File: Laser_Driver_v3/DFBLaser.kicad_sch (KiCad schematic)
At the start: 30 parts, among them Q15 IRLML6344TRPBF, Q16 IRLML6344TRPBF, U23 OPA192, U24 OPA192

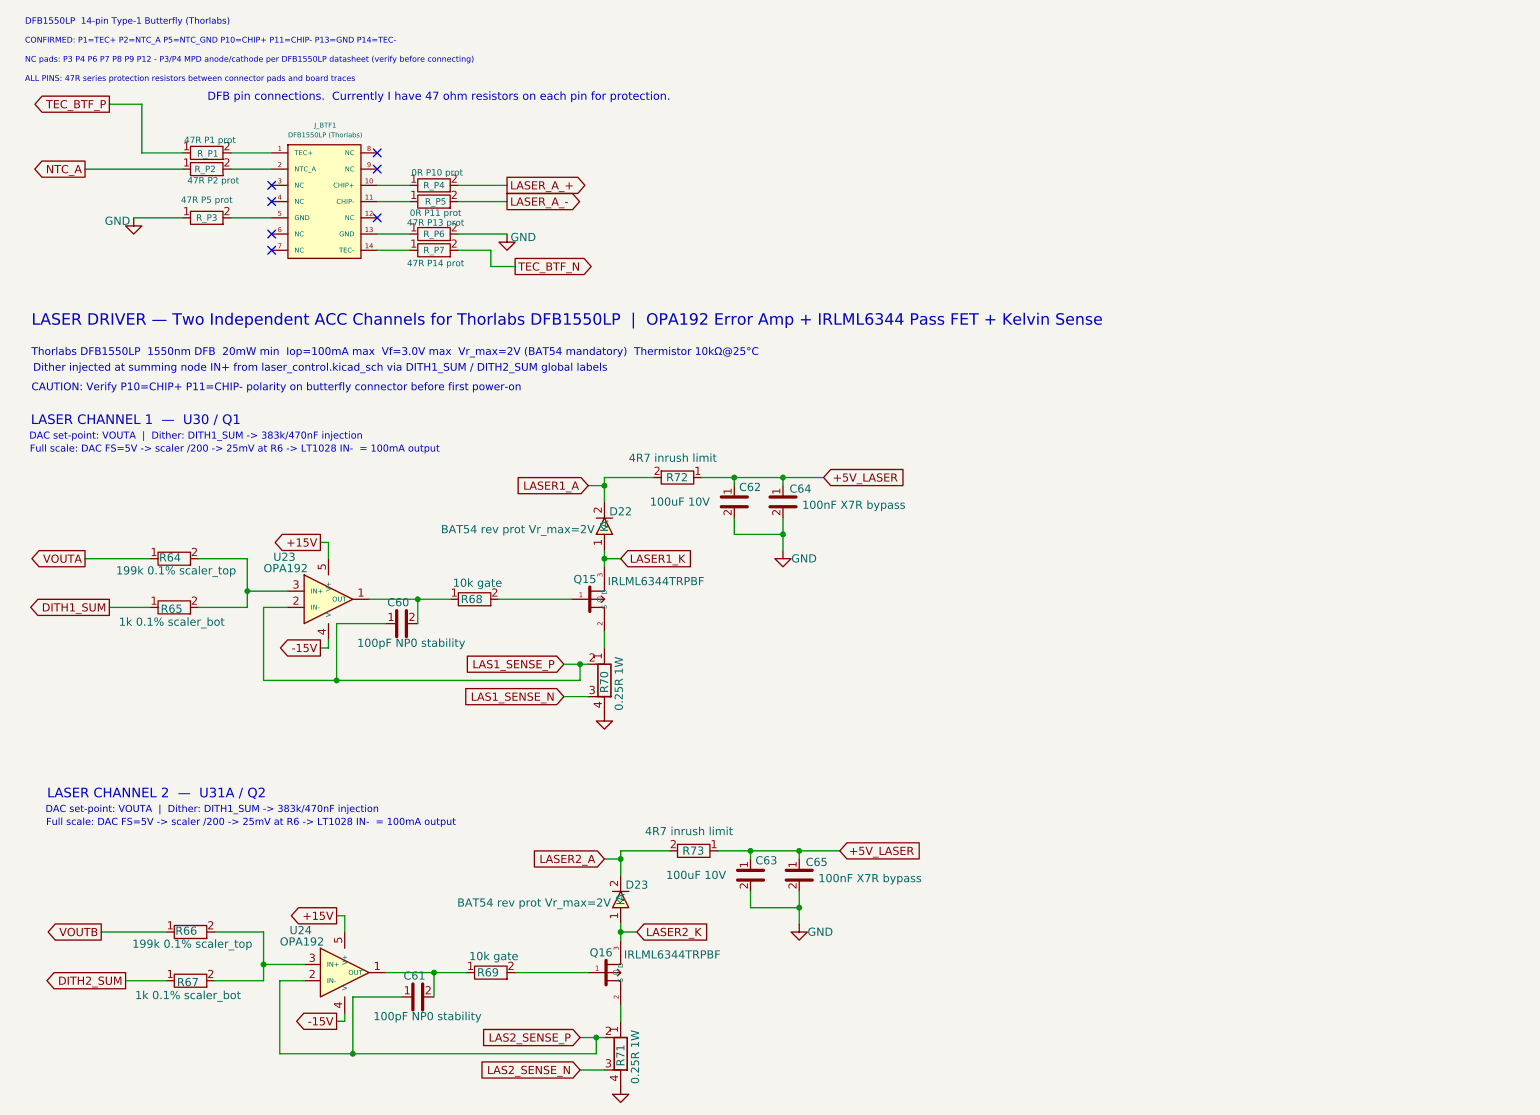
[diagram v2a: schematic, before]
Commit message: Update names, footprints, values, and created BOM
Updated files names, foot prints, component values, parts.
Assigned values from Digikey catalog.
Created CSV BOMs for each schematic.
Including a Power analysis now for all components.
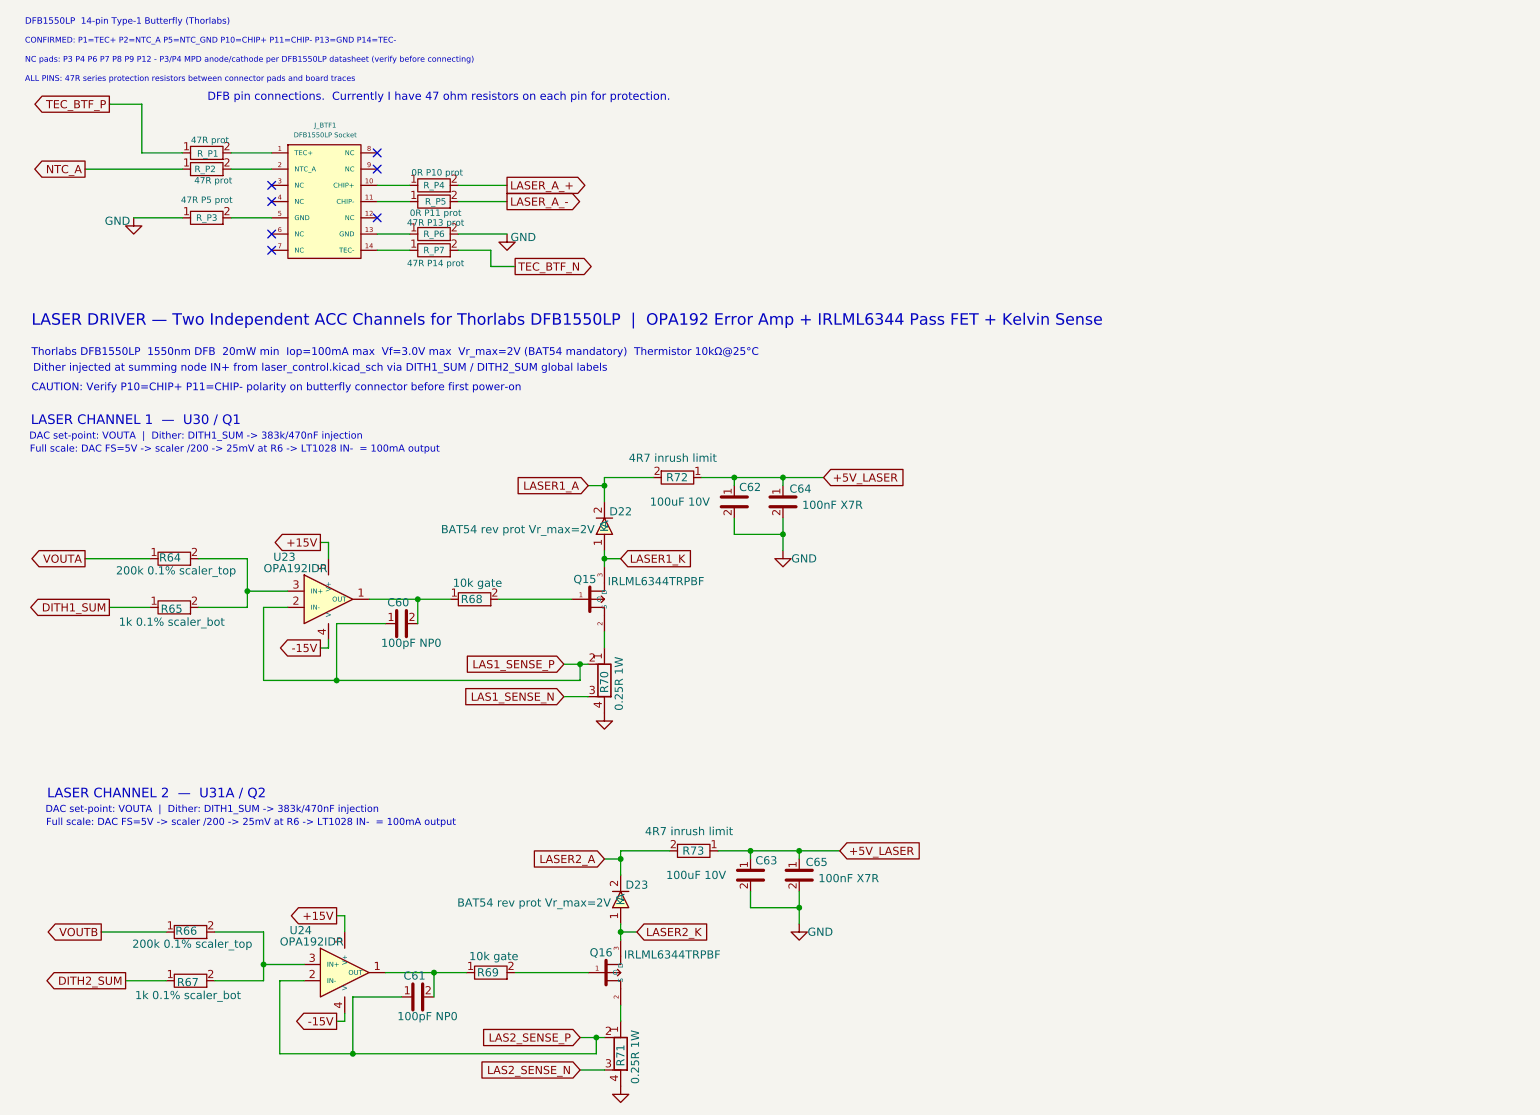
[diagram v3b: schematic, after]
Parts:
- C60, C61: value 100pF NP0 stability -> 100pF NP0; footprint Capacitor_SMD:C_0402_1005Metric -> Capacitor_SMD:C_0805_2012Metric_Pad1.18x1.45mm_HandSolder
- C64, C65: value 100nF X7R bypass -> 100nF X7R; footprint Capacitor_SMD:C_0402_1005Metric -> Capacitor_SMD:C_0805_2012Metric_Pad1.18x1.45mm_HandSolder
- J_BTF1: value DFB1550LP (Thorlabs) -> DFB1550LP Socket; footprint Connector_PinHeader_2.54mm:PinHeader_2x07_P2.54mm_Vertical -> Connector_PinSocket_2.54mm:PinSocket_2x07_P2.54mm_Vertical
- R64, R66: value 199k 0.1% scaler_top -> 200k 0.1% scaler_top
- R68, R69, R_P3, R_P4, R_P5, R_P6, R_P7: footprint Resistor_SMD:R_0402_1005Metric -> Resistor_SMD:R_0805_2012Metric_Pad1.20x1.40mm_HandSolder
- R_P1: value 47R P1 prot -> 47R prot; footprint Resistor_SMD:R_0402_1005Metric -> Resistor_SMD:R_0805_2012Metric_Pad1.20x1.40mm_HandSolder
- R_P2: value 47R P2 prot -> 47R prot; footprint Resistor_SMD:R_0402_1005Metric -> Resistor_SMD:R_0805_2012Metric_Pad1.20x1.40mm_HandSolder
- U23, U24: value OPA192 -> OPA192IDR; footprint Package_SO:SOIC-5-6_4.4x3.6mm_P1.27mm -> Package_SO:SOIC-8_3.9x4.9mm_P1.27mm
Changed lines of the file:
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@@
 			)
 		)
-		(property "Value" "47R P1 prot"
+		(property "Value" "47R prot"
 			(at 44.95 33.56 90)
 			(show_name no)
@@
 			)
 		)
-		(property "Footprint" "Resistor_SMD:R_0402_1005Metric"
+		(property "Footprint" "Resistor_SMD:R_0805_2012Metric_Pad1.20x1.40mm_HandSolder"
 			(at -285.55 73.56 0)
 			(hide yes)
@@
 			)
 		)
-		(property "Footprint" "Resistor_SMD:R_0402_1005Metric"
+		(property "Footprint" "Resistor_SMD:R_0805_2012Metric_Pad1.20x1.40mm_HandSolder"
 			(at 88.9 163.83 0)
 			(hide yes)
@@
 			)
 		)
-		(property "Value" "100pF NP0 stability"
+		(property "Value" "100pF NP0"
 			(at 76.454 112.268 90)
 			(show_name no)
@@
 			)
 		)
-		(property "Footprint" "Capacitor_SMD:C_0402_1005Metric"
+		(property "Footprint" "Capacitor_SMD:C_0805_2012Metric_Pad1.18x1.45mm_HandSolder"
 			(at 74.93 109.22 0)
 			(hide yes)
@@
 			)
 		)
-		(property "Value" "OPA192"
+		(property "Value" "OPA192IDR"
 			(at 53.34 100.584 0)
 			(show_name no)
@@
 			)
 		)
-		(property "Footprint" "Package_SO:SOIC-5-6_4.4x3.6mm_P1.27mm"
+		(property "Footprint" "Package_SO:SOIC-8_3.9x4.9mm_P1.27mm"
 			(at 68.326 87.884 0)
 			(hide yes)
@@
 			)
 		)
-		(property "Footprint" "Resistor_SMD:R_0402_1005Metric"
+		(property "Footprint" "Resistor_SMD:R_0805_2012Metric_Pad1.20x1.40mm_HandSolder"
 			(at -261.99 130.26 0)
 			(hide yes)
@@
 			)
 		)
-		(property "Value" "100nF X7R bypass"
+		(property "Value" "100nF X7R"
 			(at 140.16 149.09 0)
 			(show_name no)
@@
 			)
 		)
-		(property "Footprint" "Capacitor_SMD:C_0402_1005Metric"
+		(property "Footprint" "Capacitor_SMD:C_0805_2012Metric_Pad1.18x1.45mm_HandSolder"
 			(at 137.16 148.59 0)
 			(hide yes)
@@
 			)
 		)
-		(property "Value" "100pF NP0 stability"
+		(property "Value" "100pF NP0"
 			(at 78.994 170.688 90)
 			(show_name no)
@@
 			)
 		)
-		(property "Footprint" "Capacitor_SMD:C_0402_1005Metric"
+		(property "Footprint" "Capacitor_SMD:C_0805_2012Metric_Pad1.18x1.45mm_HandSolder"
 			(at 77.47 167.64 0)
 			(hide yes)
@@
 			)
 		)
-		(property "Value" "47R P2 prot"
+		(property "Value" "47R prot"
 			(at 45.466 39.878 90)
 			(show_name no)
@@
 			)
 		)
-		(property "Footprint" "Resistor_SMD:R_0402_1005Metric"
+		(property "Footprint" "Resistor_SMD:R_0805_2012Metric_Pad1.20x1.40mm_HandSolder"
 			(at -288.55 76.1 0)
 			(hide yes)
@@
 			)
 		)
-		(property "Value" "199k 0.1% scaler_top"
+		(property "Value" "200k 0.1% scaler_top"
 			(at 51.59 159.354 90)
 			(show_name no)
@@
 			)
 		)
-		(property "Value" "100nF X7R bypass"
+		(property "Value" "100nF X7R"
 			(at 137.62 90.67 0)
 			(show_name no)
@@
 			)
 		)
-		(property "Footprint" "Capacitor_SMD:C_0402_1005Metric"
+		(property "Footprint" "Capacitor_SMD:C_0805_2012Metric_Pad1.18x1.45mm_HandSolder"
 			(at 134.62 90.17 0)
 			(hide yes)
@@
 			)
 		)
-		(property "Value" "DFB1550LP (Thorlabs)"
+		(property "Value" "DFB1550LP Socket"
 			(at 62.992 32.766 0)
 			(show_name no)
@@
 			)
 		)
-		(property "Footprint" "Connector_PinHeader_2.54mm:PinHeader_2x07_P2.54mm_Vertical"
+		(property "Footprint" "Connector_PinSocket_2.54mm:PinSocket_2x07_P2.54mm_Vertical"
 			(at 2.23 -294.82 0)
 			(hide yes)
@@
 			)
 		)
-		(property "Footprint" "Resistor_SMD:R_0402_1005Metric"
+		(property "Footprint" "Resistor_SMD:R_0805_2012Metric_Pad1.20x1.40mm_HandSolder"
 			(at -297.55 83.72 0)
 			(hide yes)
@@
 			)
 		)
-		(property "Footprint" "Resistor_SMD:R_0402_1005Metric"
+		(property "Footprint" "Resistor_SMD:R_0805_2012Metric_Pad1.20x1.40mm_HandSolder"
 			(at -249.99 122.64 0)
 			(hide yes)
@@
 			)
 		)
-		(property "Value" "199k 0.1% scaler_top"
+		(property "Value" "200k 0.1% scaler_top"
 			(at 49.05 100.934 90)
 			(show_name no)
@@
 			)
 		)
-		(property "Value" "OPA192"
+		(property "Value" "OPA192IDR"
 			(at 55.88 159.004 0)
 			(show_name no)
@@
 			)
 		)
-		(property "Footprint" "Package_SO:SOIC-5-6_4.4x3.6mm_P1.27mm"
+		(property "Footprint" "Package_SO:SOIC-8_3.9x4.9mm_P1.27mm"
 			(at 70.866 146.304 0)
 			(hide yes)
@@
 			)
 		)
-		(property "Footprint" "Resistor_SMD:R_0402_1005Metric"
+		(property "Footprint" "Resistor_SMD:R_0805_2012Metric_Pad1.20x1.40mm_HandSolder"
 			(at -264.99 132.8 0)
 			(hide yes)
@@
 			)
 		)
-		(property "Footprint" "Resistor_SMD:R_0402_1005Metric"
+		(property "Footprint" "Resistor_SMD:R_0805_2012Metric_Pad1.20x1.40mm_HandSolder"
 			(at 86.36 105.41 0)
 			(hide yes)
@@
 			)
 		)
-		(property "Footprint" "Resistor_SMD:R_0402_1005Metric"
+		(property "Footprint" "Resistor_SMD:R_0805_2012Metric_Pad1.20x1.40mm_HandSolder"
 			(at -252.99 125.18 0)
 			(hide yes)

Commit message: first placement of all components on pcb.
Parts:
- removed R_P1, R_P2: 47R prot, Resistor_SMD:R_0805_2012Metric_Pad1.20x1.40mm_HandSolder, symbol Device:R
- removed R_P3: 47R P5 prot, Resistor_SMD:R_0805_2012Metric_Pad1.20x1.40mm_HandSolder, symbol Device:R
- removed R_P4: 0R P10 prot, Resistor_SMD:R_0805_2012Metric_Pad1.20x1.40mm_HandSolder, symbol Device:R
- removed R_P5: 0R P11 prot, Resistor_SMD:R_0805_2012Metric_Pad1.20x1.40mm_HandSolder, symbol Device:R
- removed R_P6: 47R P13 prot, Resistor_SMD:R_0805_2012Metric_Pad1.20x1.40mm_HandSolder, symbol Device:R
- removed R_P7: 47R P14 prot, Resistor_SMD:R_0805_2012Metric_Pad1.20x1.40mm_HandSolder, symbol Device:R
- added J_BTF2: DFB1550LP #2 Socket, Connector_PinSocket_2.54mm:PinSocket_2x07_P2.54mm_Vertical, symbol Connector:Conn_02x07_Odd_Even
- added R104, R105, R106, R107, R108, R109, R110, R111, R112, R113, R114, R115, R116, R117: 47R prot, Resistor_SMD:R_0805_2012Metric_Pad1.20x1.40mm_HandSolder, symbol Device:R
- J_BTF1: value DFB1550LP Socket -> DFB1550LP #1 Socket
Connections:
- net at J_BTF1.1 (TEC+): now also R104.2
- net at J_BTF1.13 (GND): now also R109.1
- net at J_BTF1.2 (NTC_A): now also R105.2
- net at J_BTF1.10 (CHIP+): now also R107.1
- net at J_BTF1.11 (CHIP-): now also R108.1
- net at J_BTF1.14 (TEC-): now also R110.1
- net at J_BTF1.5 (NTC_GND): now also R106.2
- new net: J_BTF2.5 (NTC_GND), R113.2
- new net: J_BTF2.14 (TEC-), R117.1
- new net: J_BTF2.1 (TEC+), R111.2
- new net: J_BTF2.13 (GND), R116.1
- new net: J_BTF2.2 (NTC_A), R112.2
- new net: J_BTF2.11 (CHIP-), R115.1
- new net: J_BTF2.10 (CHIP+), R114.1
- new net AGND: R106.1, R109.2, R113.1, R116.2
- new net BTF1_LASER: R107.2
- new net BTF1_LASER_K: R108.2
- new net BTF2_LASER: R114.2
- new net BTF2_LASER_K: R115.2
- new net NTC1_A: R105.1
- new net NTC2_A: R112.1
- new net TEC1_BTF_N: R110.2
- new net TEC1_BTF_P: R104.1
- new net TEC2_BTF_N: R117.2
- new net TEC2_BTF_P: R111.1
- no-connect marks 7 -> 14
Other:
- note added: "47R series protection resistors on all confirmed pins. Laser Vr_max=2V — NEVER reverse bias."
- note added: "BUTTERFLY CONNECTORS — 2x DFB1550LP | 2x7 2.54mm ZIF sockets"
- note added: "CONFIRMED PINS: P1=TEC+ P2=NTC_A P5=NTC_GND P10=CHIP+ P11=CHIP- P13=GND P14=TEC-"
- note added: "J_BTF1 — Butterfly 1"
- note added: "J_BTF2 — Butterfly 2"
- note added: "UNCONFIRMED/NC: P3 P4 P6 P7 P8 P9 P12 — verify MPD pinout"
- note removed: "ALL PINS: 47R series protection resistors between connector pads and board traces"
- note removed: "CONFIRMED: P1=TEC+ P2=NTC_A P5=NTC_GND P10=CHIP+ P11=CHIP- P13=GND P14=TEC-"
- note removed: "DFB pin connections. Currently I have 47 ohm resistors on each pin for protection."
- note removed: "DFB1550LP 14-pin Type-1 Butterfly (Thorlabs)"
- note removed: "NC pads: P3 P4 P6 P7 P8 P9 P12 - P3/P4 MPD anode/cathode per DFB1550LP datasheet (verify before connecting)"

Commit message: Added display to schematic.  Updated BOM.
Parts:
- C62, C63: footprint Capacitor_SMD:C_1210_3225Metric -> Capacitor_SMD:C_1206_3216Metric_Pad1.33x1.80mm_HandSolder
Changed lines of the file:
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@@
 			)
 		)
-		(property "Footprint" "Capacitor_SMD:C_1210_3225Metric"
+		(property "Footprint" "Capacitor_SMD:C_1206_3216Metric_Pad1.33x1.80mm_HandSolder"
 			(at 129.54 148.59 0)
 			(hide yes)
@@
 			)
 		)
-		(property "Footprint" "Capacitor_SMD:C_1210_3225Metric"
+		(property "Footprint" "Capacitor_SMD:C_1206_3216Metric_Pad1.33x1.80mm_HandSolder"
 			(at 127 90.17 0)
 			(hide yes)
